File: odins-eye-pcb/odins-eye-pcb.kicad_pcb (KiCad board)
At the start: 4 copper layers, 102 x 55 mm, 11 parts, among them J2 TF-LUNA CONNECTOR, J3 POWER USB-C, J4 GYROSCOPE-CONNECTOR

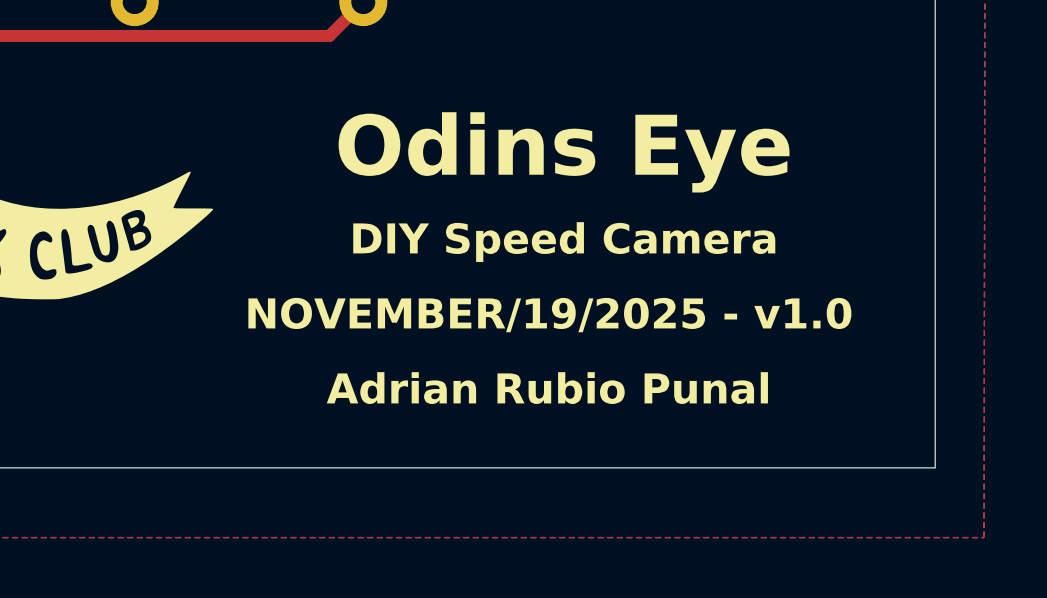
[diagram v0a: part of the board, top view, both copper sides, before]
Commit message: Changes to the 3D case
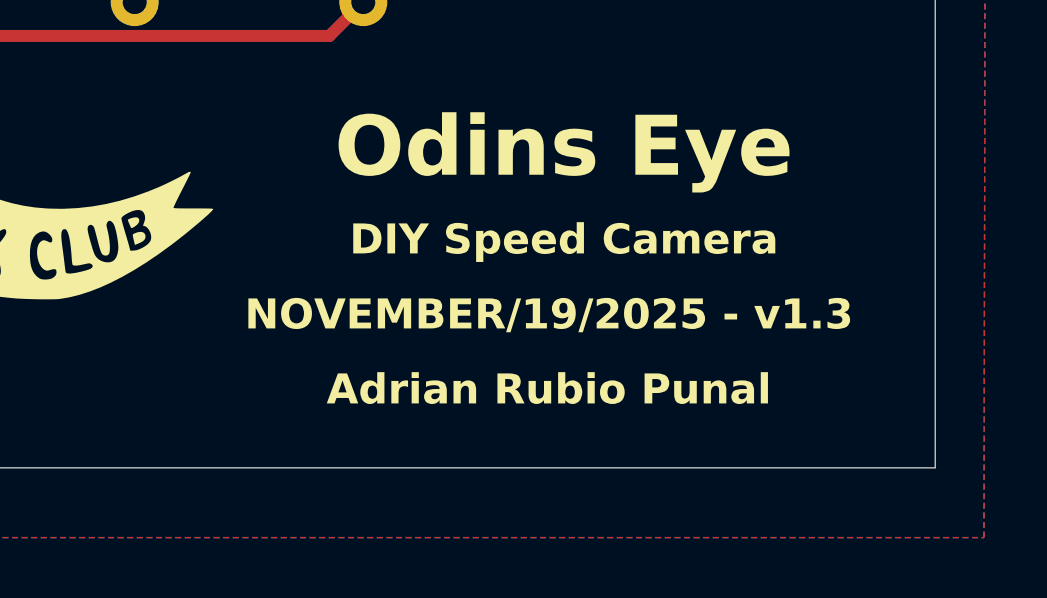
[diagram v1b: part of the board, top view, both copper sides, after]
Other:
- board text added: "NOVEMBER/19/2025 - v1.3"
- board text removed: "NOVEMBER/19/2025 - v1.0"
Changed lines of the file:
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@@
 			(drillshape 0)
 			(scaleselection 1)
-			(outputdirectory "gerbers/odins-eye-pcb-v1.2/")
+			(outputdirectory "gerbers/odins-eye-v1.3/")
 		)
 	)
@@
 		)
 	)
-	(gr_text "NOVEMBER/19/2025 - v1.0"
+	(gr_text "NOVEMBER/19/2025 - v1.3"
 		(at 186.5 115 0)
 		(layer "F.SilkS")
@@
 		(min_thickness 0.25)
 		(filled_areas_thickness no)
-		(fill yes
+		(fill
 			(thermal_gap 0.5)
 			(thermal_bridge_width 0.5)

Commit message: Add PCB v1.5
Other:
- board text added: "NOVEMBER/19/2025 - v1.4"
- board text removed: "NOTE: USB-C NPTH-GND clearance is 0.194 mm. JLCPCB spec=0.20 mm. Within tolerance. DRC warnings expected."
- board text removed: "NOVEMBER/19/2025 - v1.3"
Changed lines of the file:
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@@
 		(date "2025-11-24")
 		(rev "0")
+		(comment 4 "AISLER Project ID: MTZEQACE")
 	)
 	(layers
@@
 		(13 "F.Paste" user)
 		(15 "B.Paste" user)
-		(5 "F.SilkS" user "F.Silkscreen")
-		(7 "B.SilkS" user "B.Silkscreen")
+		(5 "F.SilkS" user)
+		(7 "B.SilkS" user)
 		(1 "F.Mask" user)
 		(3 "B.Mask" user)
-		(19 "Cmts.User" user "User.Comments")
 		(25 "Edge.Cuts" user)
 		(27 "Margin" user)
-		(31 "F.CrtYd" user "F.Courtyard")
-		(29 "B.CrtYd" user "B.Courtyard")
+		(31 "F.CrtYd" user)
+		(29 "B.CrtYd" user)
 		(35 "F.Fab" user)
 	)
@@
 			(drillshape 0)
 			(scaleselection 1)
-			(outputdirectory "gerbers/odins-eye-v1.3/")
+			(outputdirectory "gerbers/odins-eye-v1.5/")
 		)
 	)
@@
 		)
 	)
-	(gr_text "NOVEMBER/19/2025 - v1.3"
+	(gr_text "NOVEMBER/19/2025 - v1.4\n"
 		(at 186.5 115 0)
 		(layer "F.SilkS")
@@
 		)
 	)
-	(gr_text "NOTE:\nUSB-C NPTH-GND clearance is 0.194 mm.\nJLCPCB spec=0.20 mm. \nWithin tolerance. DRC warnings expected."
-		(at 192 106 0)
-		(layer "Cmts.User")
-		(effects
-			(font
-				(size 0.4 0.4)
-				(thickness 0.05)
-			)
-			(justify bottom)
-		)
-	)
 	(segment
 		(start 175.335 94.9)
@@
 		(start 192.017008 92.28)
 		(end 191.52 92.28)
-		(width 0.4)
+		(width 0.2)
 		(layer "F.Cu")
 		(net 11)
@@
 		(start 191.52 97.08)
 		(end 192.058281 97.08)
-		(width 0.4)
+		(width 0.2)
 		(layer "F.Cu")
 		(net 11)
@@
 		(start 192.058281 97.08)
 		(end 192.423 96.715281)
-		(width 0.4)
+		(width 0.2)
 		(layer "F.Cu")
 		(net 11)
@@
 		(start 192.423 96.715281)
 		(end 192.423 92.685992)
-		(width 0.4)
+		(width 0.2)
 		(layer "F.Cu")
 		(net 11)
@@
 		(start 192.423 92.685992)
 		(end 192.017008 92.28)
-		(width 0.4)
+		(width 0.2)
 		(layer "F.Cu")
 		(net 11)
@@
 		(min_thickness 0.25)
 		(filled_areas_thickness no)
-		(fill
+		(fill yes
 			(thermal_gap 0.5)
 			(thermal_bridge_width 0.5)
